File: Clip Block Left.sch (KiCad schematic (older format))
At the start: 20 parts, among them SW1 B3F-5050, SW10 B3F-5050, SW11 B3F-5050, SW12 B3F-5050, SW13 B3F-5050, SW14 B3F-5050, SW15 B3F-5050, SW16 B3F-5050, SW2 B3F-5050, SW3 B3F-5050, SW4 B3F-5050, SW5 B3F-5050, SW6 B3F-5050, SW7 B3F-5050, SW8 B3F-5050, SW9 B3F-5050, U1 CD74HC4067M

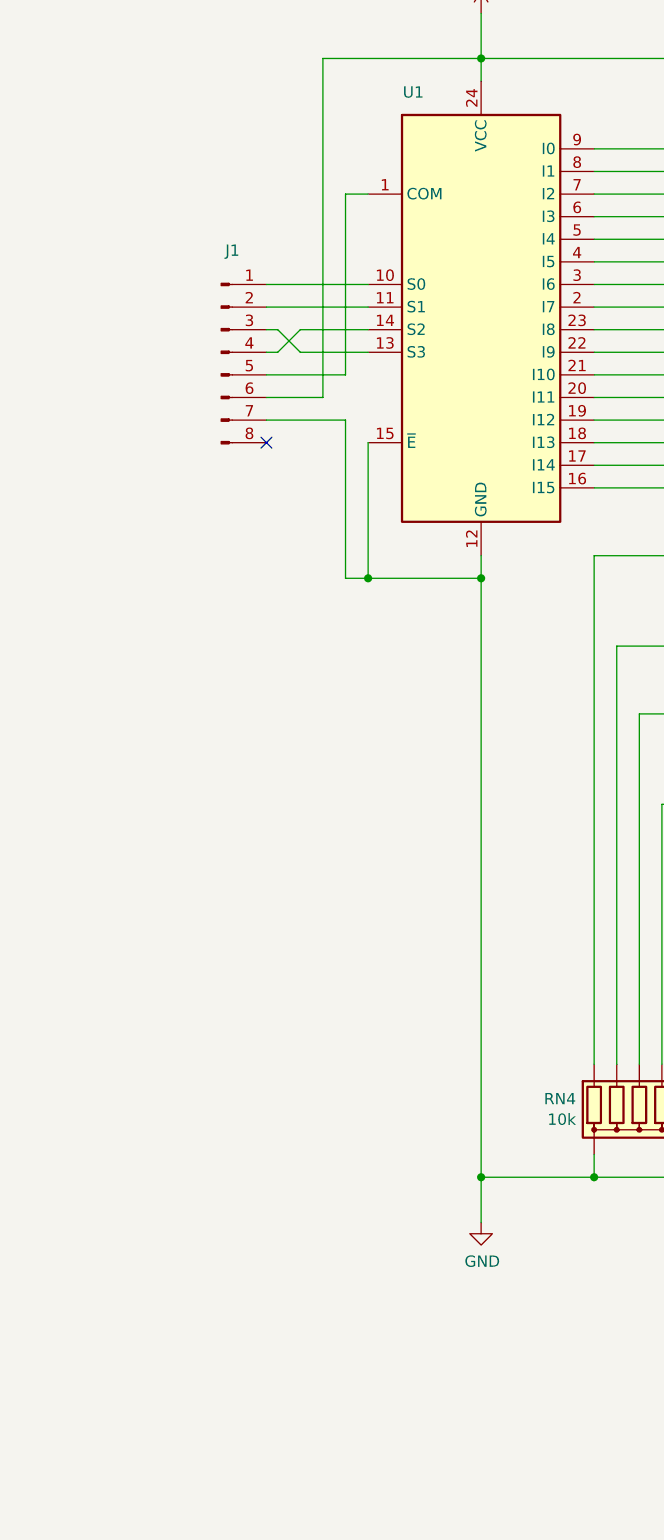
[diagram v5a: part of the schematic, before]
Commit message: Further cleanup and placement
Removed all the connectors to the rails as they're irrelevant to the top boards.

Added all the support headers.

Need to work out the correct routing for the headers but the placement is correct.
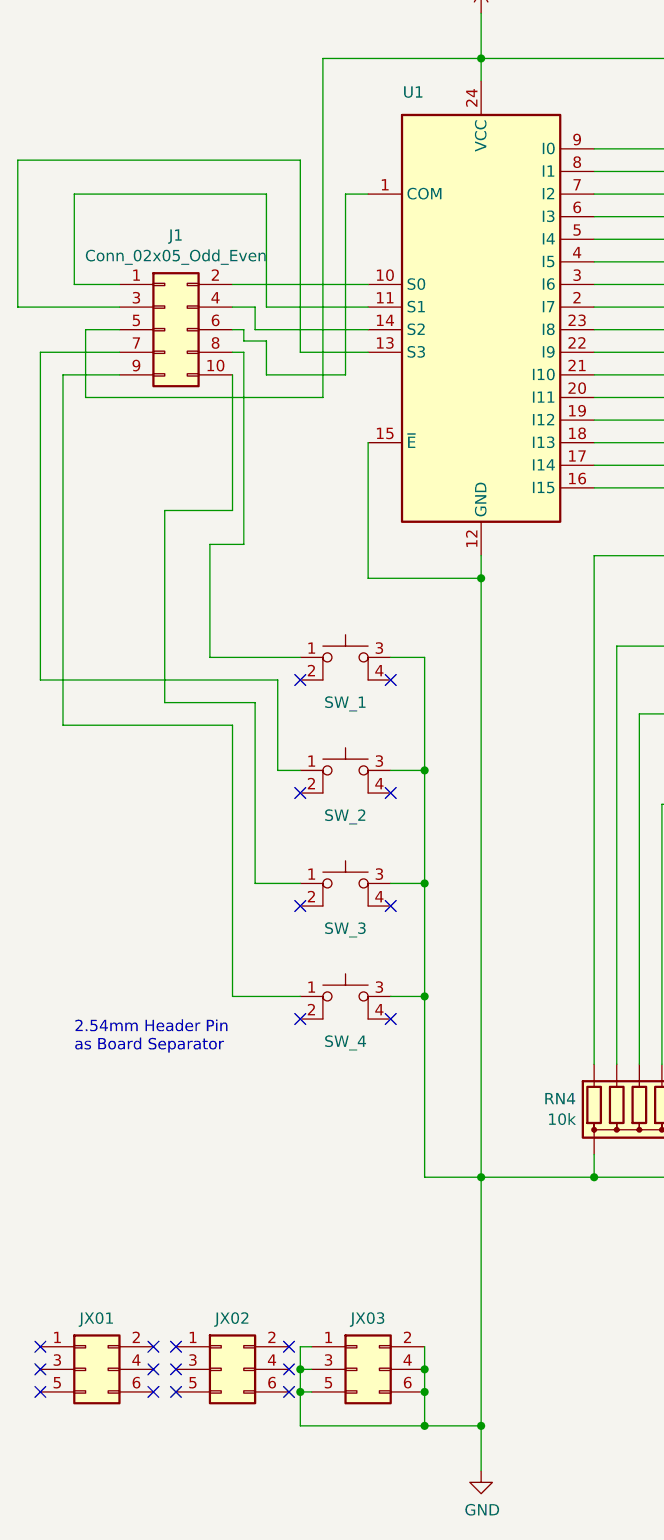
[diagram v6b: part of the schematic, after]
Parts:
- removed J1: ~, cunabulapress-footprints:Connector_TE_Connectivity_Micro-MaTch_8_Position_Female, symbol Connector:Conn_01x08_Male
- added J1: Conn_02x05_Odd_Even, Connector_PinHeader_2.54mm:PinHeader_2x05_P2.54mm_Vertical, symbol Connector_Generic:Conn_02x05_Odd_Even
- added JX01, JX02, JX03: Conn_02x03_Odd_Even, Connector_PinHeader_2.54mm:PinHeader_2x03_P2.54mm_Vertical, symbol Connector_Generic:Conn_02x03_Odd_Even
- added SW_1, SW_2, SW_3, SW_4: B3F-5050, cunabulapress-footprints:Omron_B3F-5050, symbol cp_midi_control_surface_002-rescue:SW_SPST_4_PIN-sw_spst_0
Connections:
- net +5V: now also J1.5 (Pin_5)
- net GND: now also JX03.1 (Pin_1), JX03.2 (Pin_2), JX03.3 (Pin_3), JX03.4 (Pin_4), JX03.5 (Pin_5), JX03.6 (Pin_6), SW_1.3, SW_2.3, SW_3.3, SW_4.3
- net at U1.1 (COM): now also J1.6 (Pin_6)
- net at U1.10 (S0): now also J1.2 (Pin_2)
- net at U1.11 (S1): now also J1.1 (Pin_1)
- net at U1.13 (S3): now also J1.3 (Pin_3)
- net at U1.14 (S2): now also J1.4 (Pin_4)
- new net: J1.8 (Pin_8), SW_1.1 (A)
- new net: J1.7 (Pin_7), SW_2.1 (A)
- new net: J1.10 (Pin_10), SW_3.1 (A)
- new net: J1.9 (Pin_9), SW_4.1 (A)
- no-connect marks 33 -> 52
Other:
- note added: "2.54mm Header Pin\nas Board Separator"
